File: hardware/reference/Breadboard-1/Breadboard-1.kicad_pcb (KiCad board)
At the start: 2 copper layers, 50.8 x 69.9 mm, 66 parts, among them J1 Left, J2 Right, J3 ICSP, J4 Oscilloscope, J5 TTL Serial, Q31 NCE2309, Q32 NCE2309, Q33 DMN6140L-7, Q34 DMN6140L-7, Q35 DTC143ZCA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

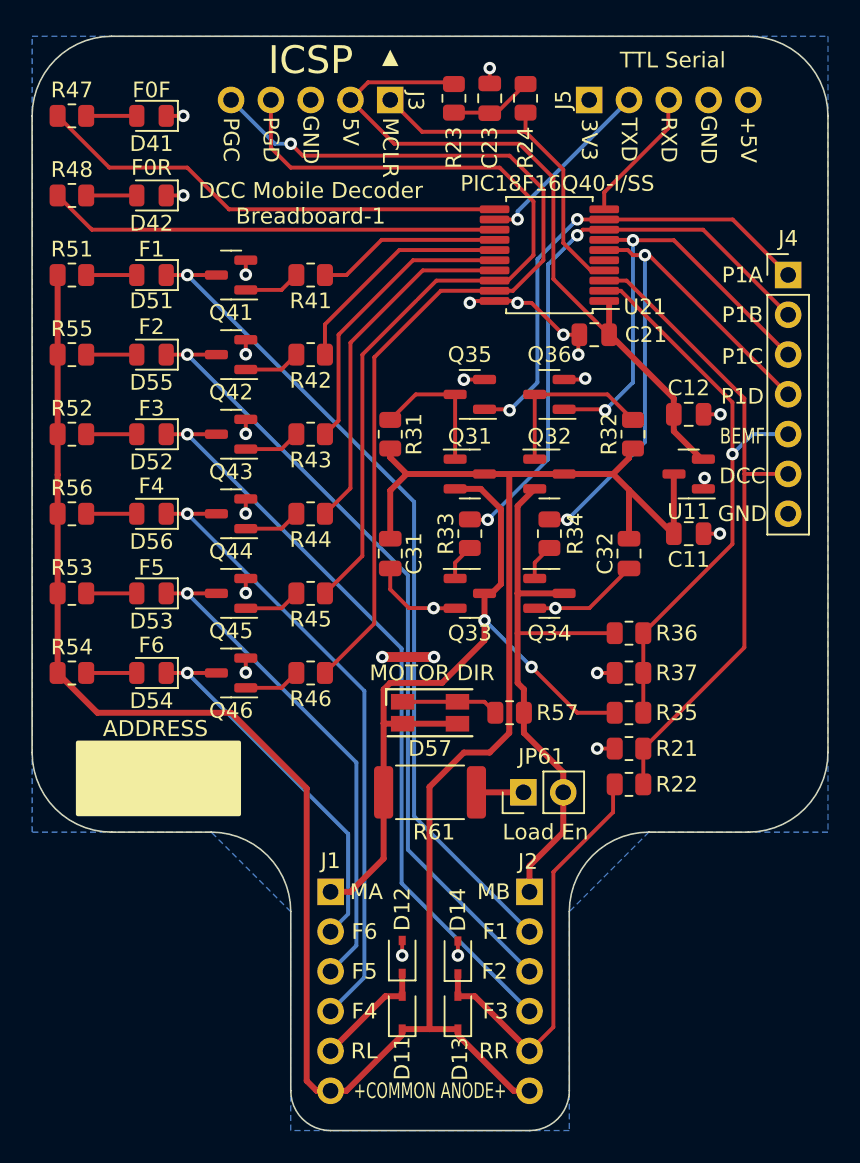
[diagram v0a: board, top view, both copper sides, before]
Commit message: Manufacturability changes.
Added 3 fiducial markers to support pick and place in volume.
Resized all the traces to be manufacturable with the popular board fabs.
Moved traces based on the new size.
Standardized vias to one size larger than the general manufacturing minimum.
Improved grounding around the CPU.
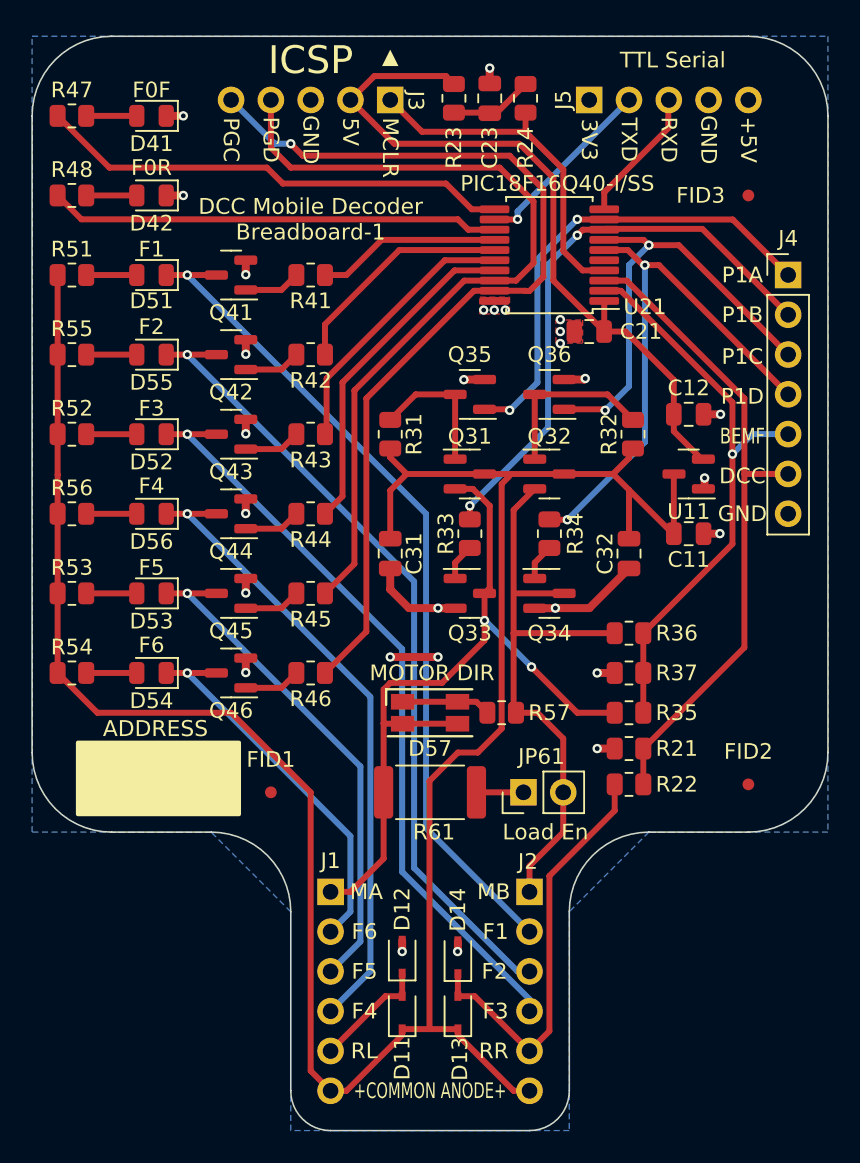
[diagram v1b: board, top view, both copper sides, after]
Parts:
- added FID1: Fiducial_0.75mm_Mask2.25mm, Fiducial:Fiducial_0.75mm_Mask2.25mm, F.Cu at (66.0, 99.1)
- added FID2: Fiducial_0.75mm_Mask2.25mm, Fiducial:Fiducial_0.75mm_Mask2.25mm, F.Cu at (96.5, 98.6)
- added FID3: Fiducial_0.75mm_Mask2.25mm, Fiducial:Fiducial_0.75mm_Mask2.25mm, F.Cu at (96.5, 61.0)
- moved R57 0.51 mm to (80.8, 94.0)
- moved C21 0.38 mm to (86.4, 69.6)
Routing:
- net GND: track 43.9 -> 34.0 mm, vias 26 -> 28
- net MOT_B: track 37.4 -> 38.7 mm
- net F4: track 22.7 -> 21.5 mm
- net F3: track 18.6 -> 17.4 mm
- net MOT_A: track 50.8 -> 49.7 mm
- net +5V: track 46.3 -> 47.2 mm
- net Vdrive: track 153.9 -> 153.2 mm
- net P1B: track 39.0 -> 38.3 mm
- net P1D: track 35.7 -> 35.0 mm
- net PGC/F6: track 61.6 -> 61.0 mm
- net PGD/F5: track 54.3 -> 53.7 mm
- net Net-(D57-Pad1): track 6.21 -> 5.70 mm
- added copper zone on F.Cu, net GND

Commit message: Updates based on feedback from JLCPCB online tools.
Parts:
- removed FID1, FID2, FID3: Fiducial_0.75mm_Mask2.25mm, Fiducial:Fiducial_0.75mm_Mask2.25mm
- added REF**: JLCPCB Assembly Tooling Hole, DCC Project Footprints:JLCPCB Assembly Tooling Hole, F.Cu at (99.1, 94.0)
- added REF**: JLCPCB Assembly Tooling Hole, DCC Project Footprints:JLCPCB Assembly Tooling Hole, F.Cu at (99.1, 58.4)
- added REF**: JLCPCB Assembly Tooling Hole, DCC Project Footprints:JLCPCB Assembly Tooling Hole, F.Cu at (55.9, 73.7)
- D11, D12, D13, D14: value B5819WS -> 1N5819
- Q33, Q34: value DMN6140L-7 -> DMN6140
- Q41, Q42, Q43, Q44, Q45, Q46: value 2N7002K -> 2N7002
- R22, R35, R36: value 6K6 -> 6K65

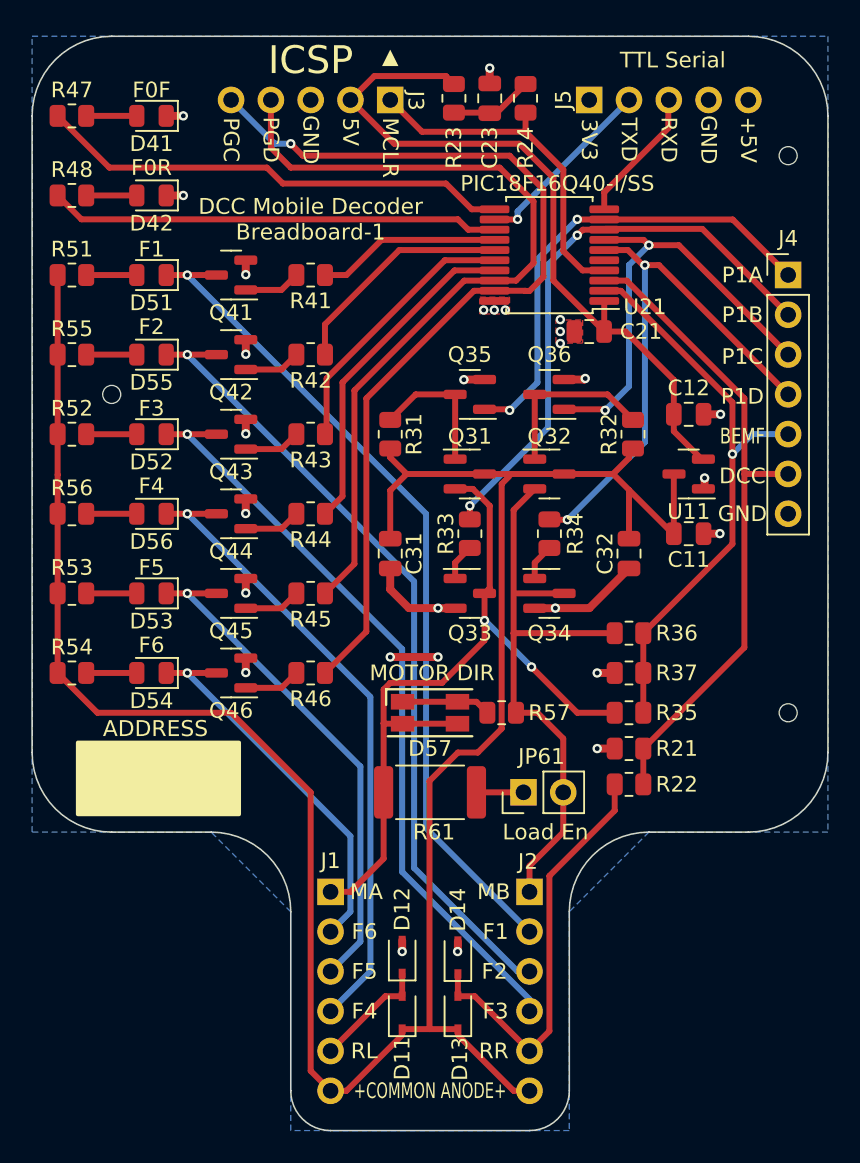
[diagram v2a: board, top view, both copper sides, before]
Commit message: Pile of minor corrections for sharing and production.
1. Remove .DS_Store files mistakenly added.
2. Correctly relatively path project footprints and symbols.
3. Add footprint for JLCPCB's required tooling hole to use their assembly service.
4. Tweak a few tracks and description placements to enhance readability.
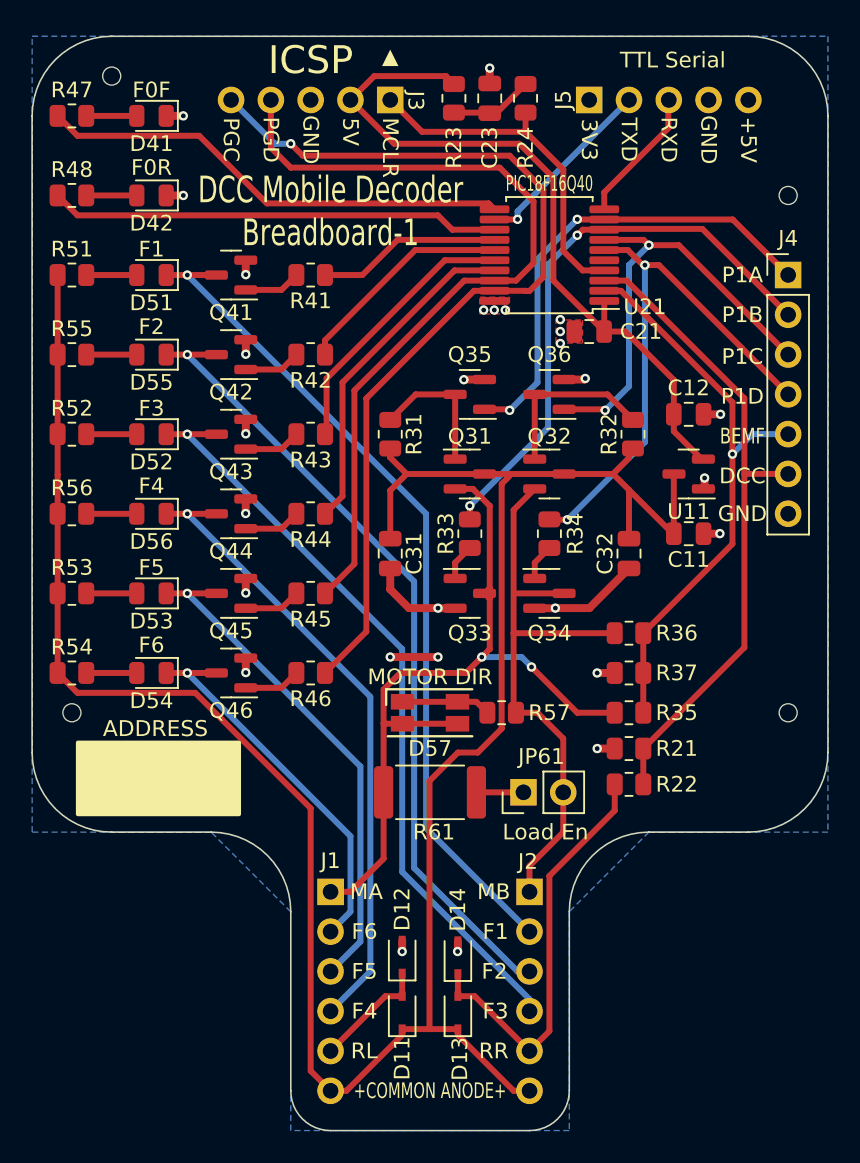
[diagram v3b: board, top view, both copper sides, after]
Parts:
- added REF**: JLCPCB Assembly Tooling Hole, DCC Project Footprints:JLCPCB Assembly Tooling Hole, F.Cu at (55.9, 53.3)
- U21: value PIC18F16Q40-I/SS -> PIC18F16Q40
- moved REF** 20.5 mm to (53.3, 94.0)
- moved REF** 2.54 mm to (99.1, 61.0)
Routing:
- net F2: track 14.7 -> 14.1 mm
- net Vdrive: track 153.2 -> 152.6 mm

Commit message: Moved CALCULATIONS to a spreadsheet.
Moved the calculations into a spreadsheet so that the values would
dynamically change when components needed to be updated.  Used the
dynamic capabilities along with the JLCPCB parts list to update
resistor values to have more common values and use JLCPCB basic
parts values.

Determined also that the calculations on the DCC input were wrong
in the previous file and added D21 to clamp the input and protect
the PIC.

Fixed the "Values" in the BOM so the components group properly.
This required also updating a number of silk screen items.

Added the copyright notice and URL to the back of the board.
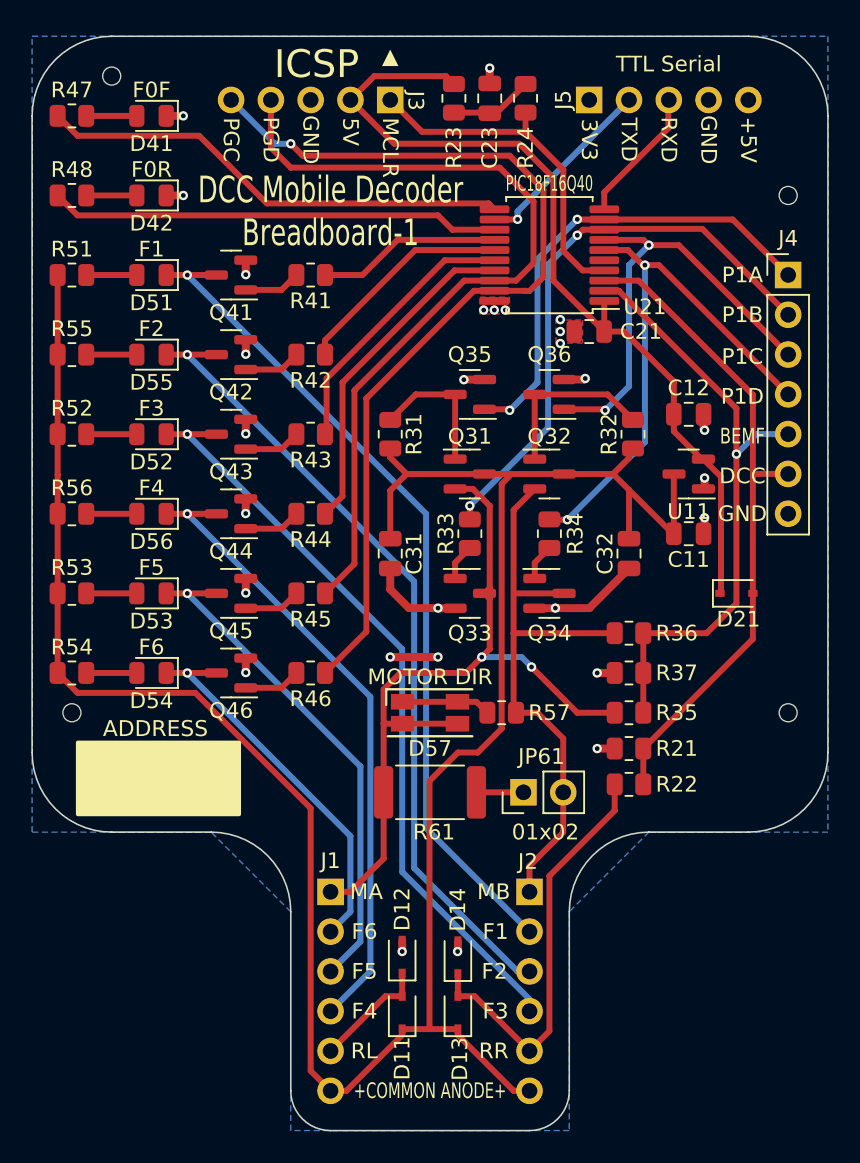
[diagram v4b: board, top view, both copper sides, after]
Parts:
- added D21: 1N5819, Diode_SMD:D_SOD-323, F.Cu at (95.8, 86.4)
- D41: value F0F -> White LED
- D42: value F0R -> White LED
- D51: value F1 -> White LED
- D52: value F3 -> White LED
- D53: value F5 -> White LED
- D54: value F6 -> White LED
- D55: value F2 -> White LED
- D56: value F4 -> White LED
- D57: value MOTOR DIR -> R/G LED
- J1: value Left -> 01x06
- J2: value Right -> 01x06
- J3: value ICSP -> 01x05
- J4: value Oscilloscope -> 01x07
- J5: value TTL Serial -> 01x05S
- JP61: value Load En -> 01x02
- Q31, Q32: value NCE2309 -> SL2309
- R21: value 1K3 -> 4K7
- R22: value 6K65 -> 9K1
- R23, R31, R32: value 10K -> 9K1
- R24, R33, R34, R41, R42, R43, R44, R45, R46: value 220 -> 470R
- R35, R36: value 6K65 -> 470R
- R37, R51, R52, R53, R54, R55, R56, R57: value 1K3 -> 2K7
- R47, R48: value 470 -> 470R
- R61: value 100 -> 100R
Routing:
- net +5V: track 47.2 -> 56.2 mm
- net BackEMF: track 37.4 -> 39.6 mm
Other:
- board text added: "https://github.com/bicknell/DCC-Mobile-Decoder Licensed under the Creative Commons Attribution-NonCommercial 4.0 International Public License, see the file LICENSE for complete details."

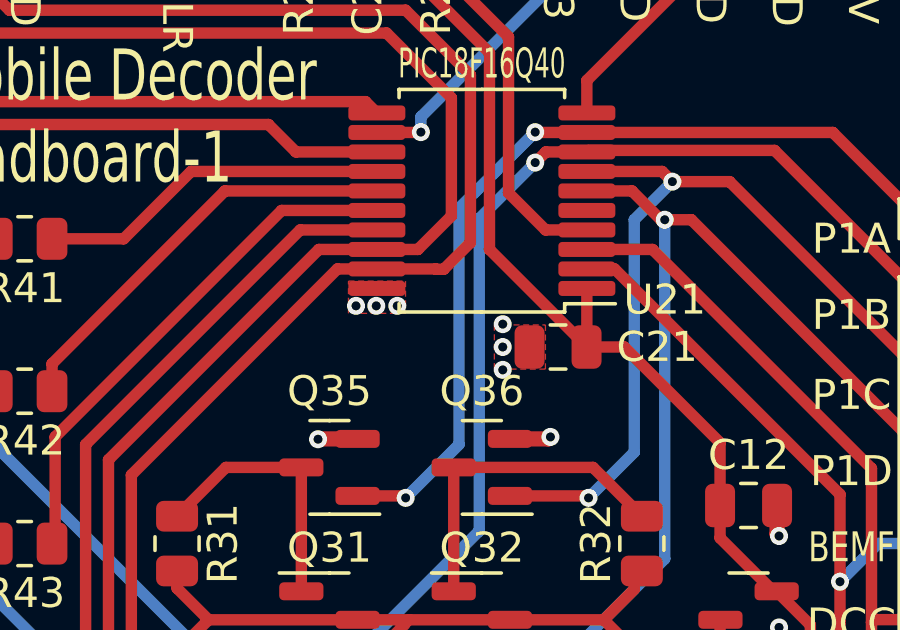
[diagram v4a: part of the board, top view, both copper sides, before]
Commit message: Added missing ground trace and regenerated image.
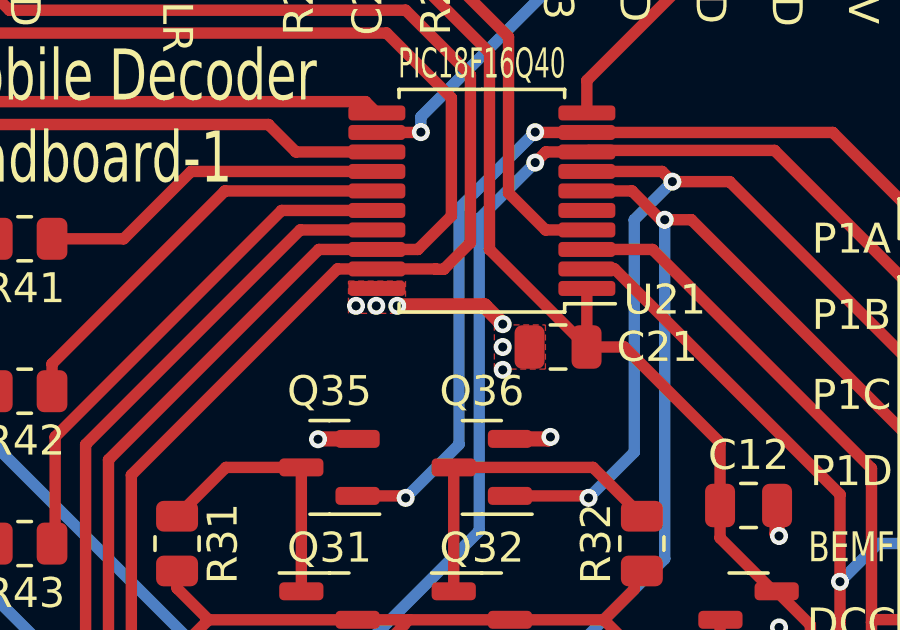
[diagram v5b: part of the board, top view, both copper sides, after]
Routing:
- net GND: track 34.0 -> 37.7 mm
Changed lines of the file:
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@@
   (segment (start 64.4398 76.1746) (end 64.4398 75.2523) (width 0.508) (layer "F.Cu") (net 15))
   (segment (start 64.4398 75.2523) (end 64.4375 75.25) (width 0.508) (layer "F.Cu") (net 15))
+  (segment (start 81 68.275) (end 83.9062 68.275) (width 0.508) (layer "F.Cu") (net 15))
   (segment (start 64.4398 86.3346) (end 64.4398 85.4123) (width 0.508) (layer "F.Cu") (net 15))
   (segment (start 73.66 90.424) (end 76.708 90.424) (width 0.508) (layer "F.Cu") (net 15))
@@
   (segment (start 73.66 86.106) (end 74.8538 87.2998) (width 0.508) (layer "F.Cu") (net 15))
   (segment (start 64.4398 85.4123) (end 64.4375 85.41) (width 0.508) (layer "F.Cu") (net 15))
+  (segment (start 83.9062 68.275) (end 84.516 68.8848) (width 0.508) (layer "F.Cu") (net 15))
   (segment (start 74.422 108.517) (end 74.422 109.22) (width 0.508) (layer "F.Cu") (net 15))
   (segment (start 79.6775 72.71) (end 78.3692 72.71) (width 0.508) (layer "F.Cu") (net 15))
